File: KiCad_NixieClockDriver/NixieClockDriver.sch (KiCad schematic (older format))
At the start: 68 parts, among them J1 Multiplexer, J2 sterowanie_lamp, J3 BOOT_0, J4 HV_OUT, J5 Barrel_Jack, J6 SWD, Q1 MPSA42, Q10 MPSA42, Q11 BC557, Q12 IRF740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

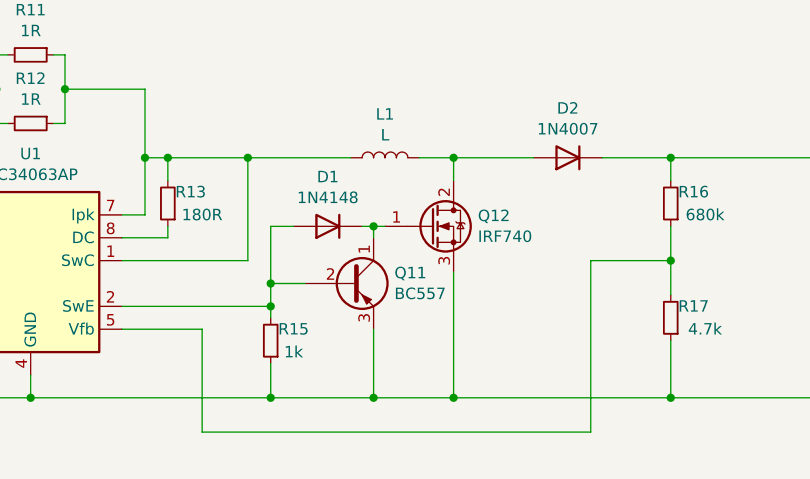
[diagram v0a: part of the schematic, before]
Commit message: Fixed reversed transistor in driver schematic
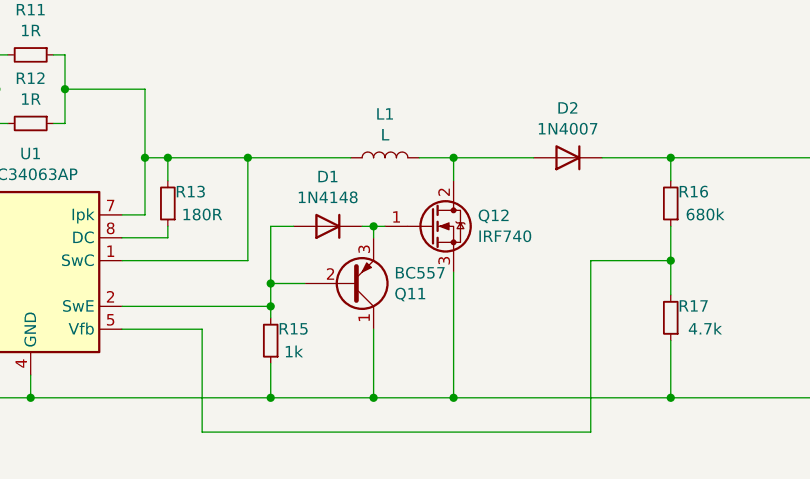
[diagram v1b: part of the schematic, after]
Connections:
- net GND: now also Q11.1 (C); no longer Q11.3 (E)
- net at D1.1 (K), Q12.1 (G): now also Q11.3 (E); no longer Q11.1 (C)
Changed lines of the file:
@@
 EESchema Schematic File Version 4
-LIBS:NixieClockDriver-cache
-EELAYER 29 0
+EELAYER 30 0
 EELAYER END
 $Descr A3 16535 11693
 encoding utf-8
 Sheet 1 1
-Title ""
+Title "Nixie Clock Driver"
 Date ""
-Rev ""
-Comp ""
+Rev "v1.1"
+Comp "Anvil Electronics"
 Comment1 ""
 Comment2 ""
@@
 F 3 "http://www.fairchildsemi.com/ds/BC/BC557.pdf" H 4650 9250 50  0001 L CNN
 	1    4650 9250
-	1    0    0    -1
-$EndComp
-$Comp
+	1    0    0    1
+$EndComp
+$Comp

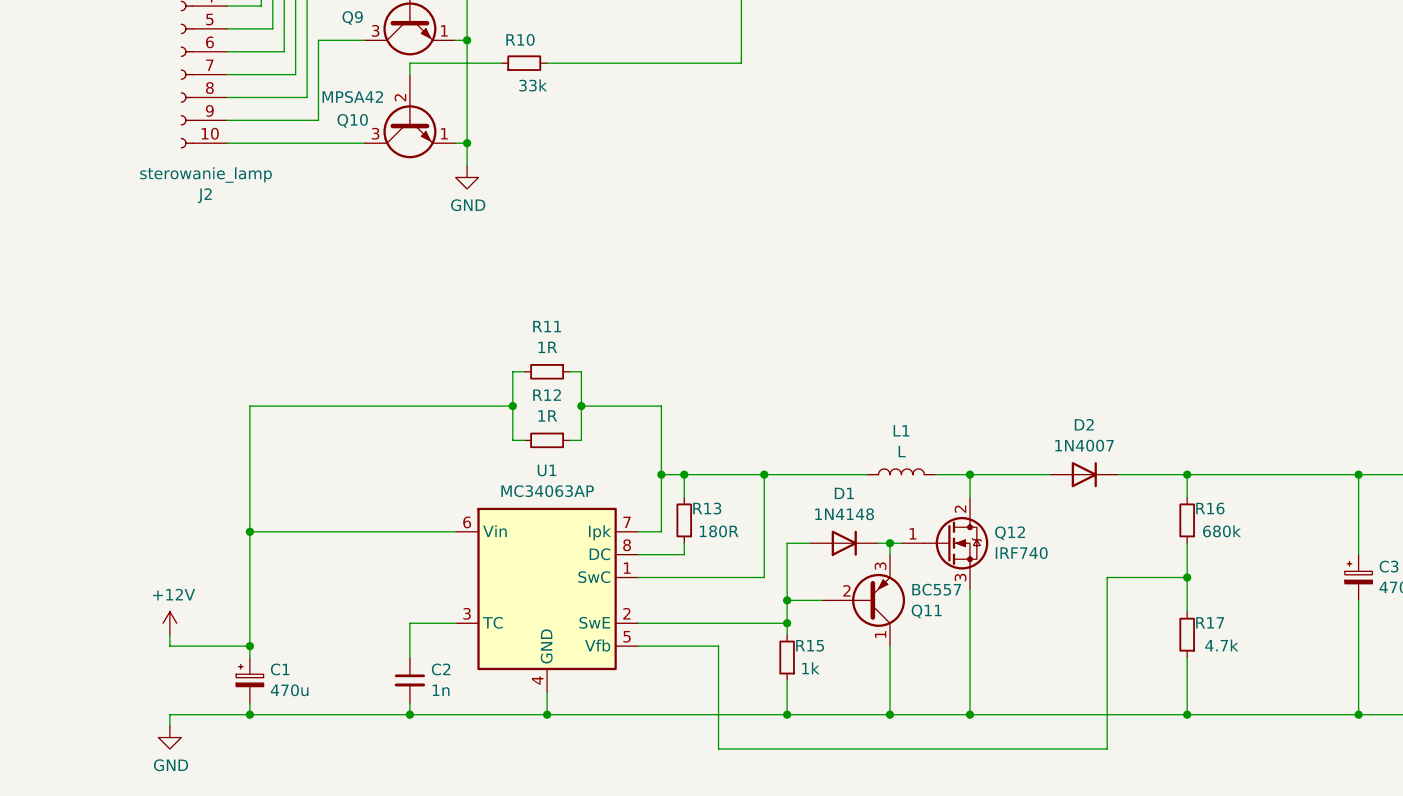
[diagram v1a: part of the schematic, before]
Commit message: Schematics in PDF
+ added schematics in PDF format for quick preview without KiCad
+ small changes in component description placemnt for better readability
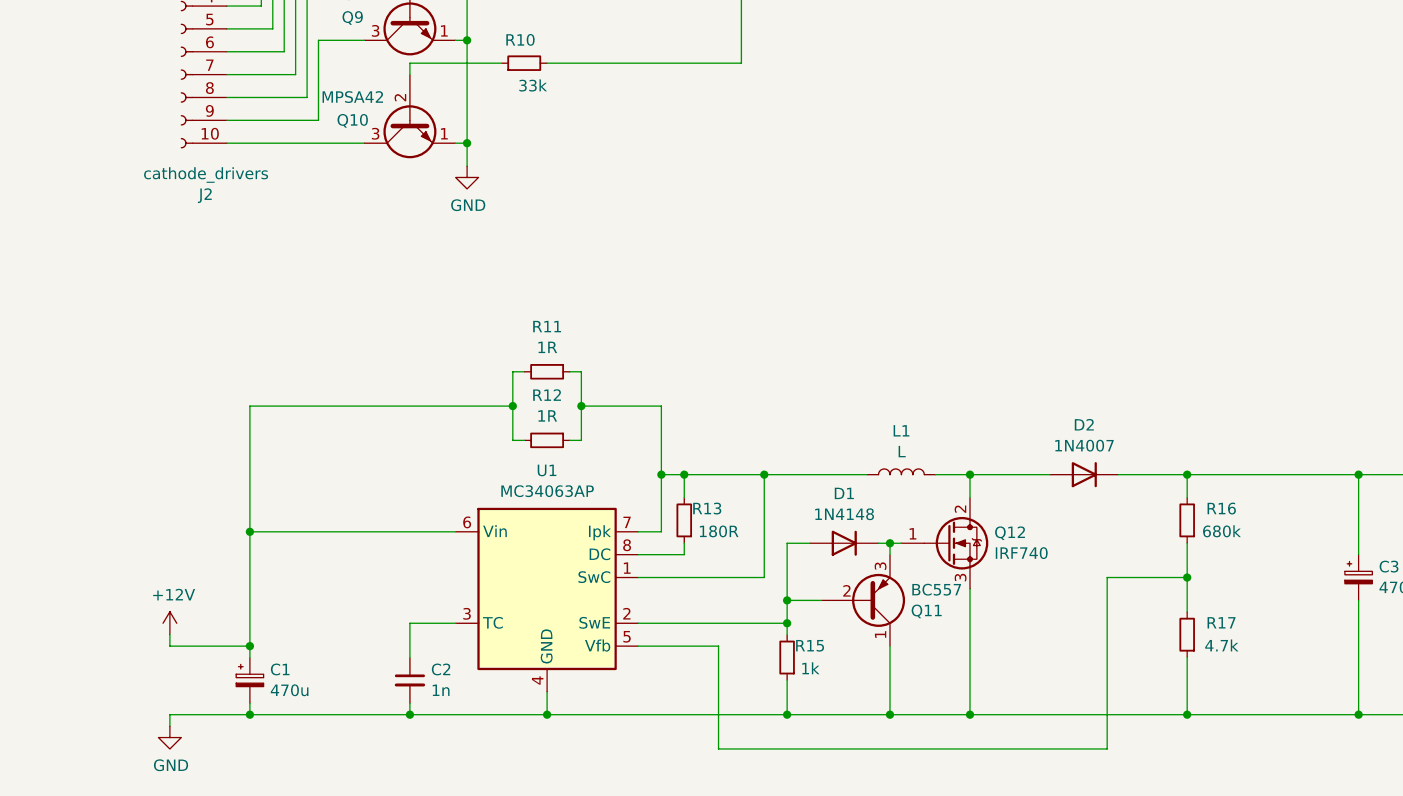
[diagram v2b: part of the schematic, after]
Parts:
- J2: value sterowanie_lamp -> cathode_drivers
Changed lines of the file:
@@
 P 1650 6750
 F 0 "J2" H 1542 6025 50  0000 C CNN
-F 1 "sterowanie_lamp" H 1542 6116 50  0000 C CNN
+F 1 "cathode_drivers" H 1542 6116 50  0000 C CNN
 F 2 "Connector_PinSocket_2.54mm:PinSocket_1x10_P2.54mm_Vertical" H 1650 6750 50  0001 C CNN
 F 3 "~" H 1650 6750 50  0001 C CNN
@@
 	4300 9350 4300 9250
 $Comp
-L Device:R_Small R16
-U 1 1 5DBE2141
-P 6050 8900
-F 0 "R16" H 5950 8850 50  0000 C CNN
-F 1 "680k" H 5900 8950 50  0000 C CNN
-F 2 "Resistor_SMD:R_1206_3216Metric" H 6050 8900 50  0001 C CNN
-F 3 "~" H 6050 8900 50  0001 C CNN
-	1    6050 8900
-	-1   0    0    1
-$EndComp
-$Comp
-L Device:R_Small R17
-U 1 1 5DBF41C0
-P 6050 9400
-F 0 "R17" H 5950 9350 50  0000 C CNN
-F 1 "4.7k" H 5900 9450 50  0000 C CNN
-F 2 "Resistor_SMD:R_1206_3216Metric" H 6050 9400 50  0001 C CNN
-F 3 "~" H 6050 9400 50  0001 C CNN
-	1    6050 9400
-	-1   0    0    1
-$EndComp
-$Comp
 L Diode:1N4007 D2
 U 1 1 5DC06DAC
@@
 Wire Wire Line
 	3300 2300 3300 2250
+$Comp
+L Device:R_Small R17
+U 1 1 5DBF41C0
+P 6050 9400
+F 0 "R17" H 5900 9350 50  0000 C CNN
+F 1 "4.7k" H 5900 9450 50  0000 C CNN
+F 2 "Resistor_SMD:R_1206_3216Metric" H 6050 9400 50  0001 C CNN
+F 3 "~" H 6050 9400 50  0001 C CNN
+	1    6050 9400
+	-1   0    0    1
+$EndComp
+$Comp
+L Device:R_Small R16
+U 1 1 5DBE2141
+P 6050 8900
+F 0 "R16" H 5900 8850 50  0000 C CNN
+F 1 "680k" H 5900 8950 50  0000 C CNN
+F 2 "Resistor_SMD:R_1206_3216Metric" H 6050 8900 50  0001 C CNN
+F 3 "~" H 6050 8900 50  0001 C CNN
+	1    6050 8900
+	-1   0    0    1
+$EndComp
 $EndSCHEMATC
